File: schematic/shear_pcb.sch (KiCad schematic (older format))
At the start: 6 parts, among them J1 MOTOR1, J2 MOTOR2, J3 LCD_CONN, U1 Teensy3.5, U2 AMIS30542, U3 AMIS30542

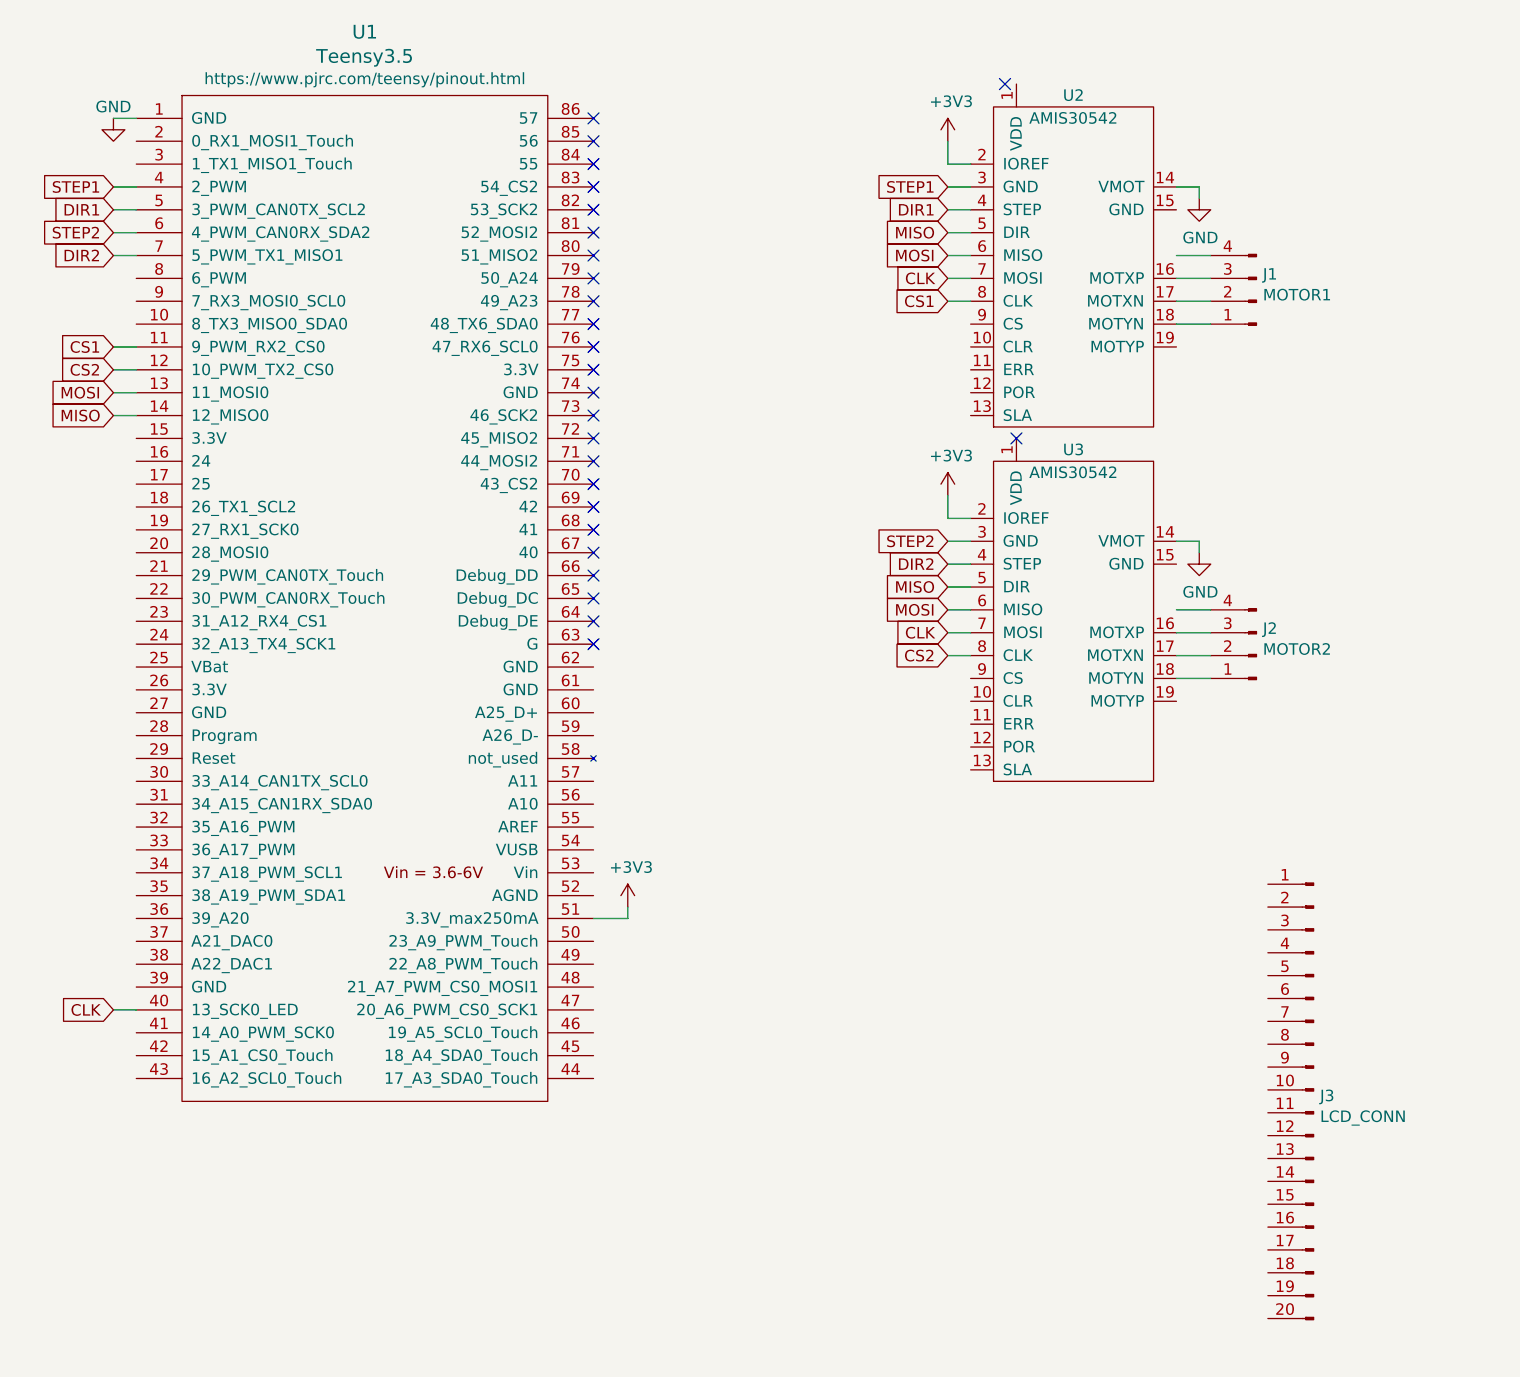
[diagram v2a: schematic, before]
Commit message: Add connectors and first pcb design
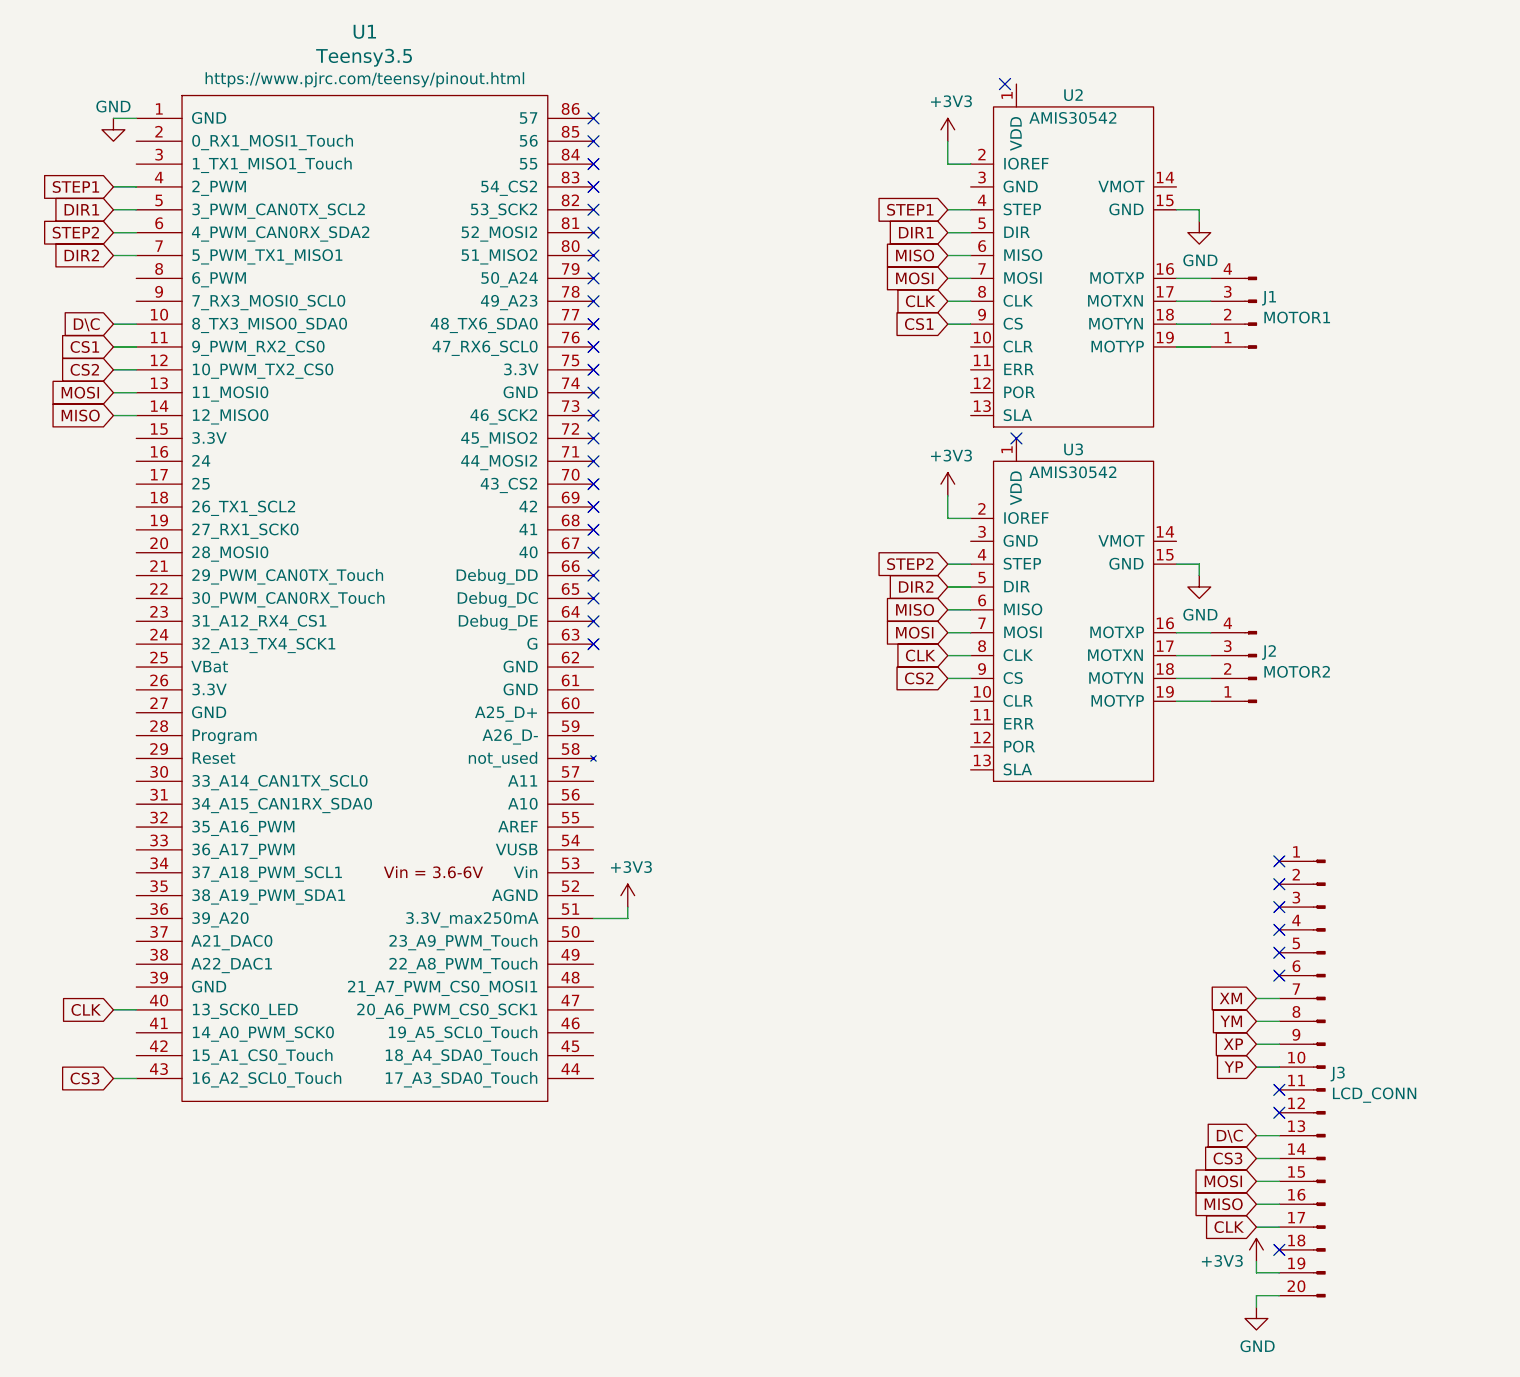
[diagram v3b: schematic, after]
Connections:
- net labels added: CS3, D\C, XM, XP, YM, YP
- wire segments 40 -> 55
- no-connect marks 26 -> 35
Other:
- moved on the sheet: J1, J2, J3
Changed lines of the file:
@@
 L power:GND #PWR0105
 U 1 1 5CCD7013
-P 9250 2950
-F 0 "#PWR0105" H 9250 2700 50  0001 C CNN
-F 1 "GND" H 9255 2777 50  0000 C CNN
-F 2 "" H 9250 2950 50  0001 C CNN
-F 3 "" H 9250 2950 50  0001 C CNN
-	1    9250 2950
+P 9250 3050
+F 0 "#PWR0105" H 9250 2800 50  0001 C CNN
+F 1 "GND" H 9255 2877 50  0000 C CNN
+F 2 "" H 9250 3050 50  0001 C CNN
+F 3 "" H 9250 3050 50  0001 C CNN
+	1    9250 3050
 	1    0    0    -1
 $EndComp
@@
 L power:GND #PWR0106
 U 1 1 5CCD743D
-P 9250 1400
-F 0 "#PWR0106" H 9250 1150 50  0001 C CNN
-F 1 "GND" H 9255 1227 50  0000 C CNN
-F 2 "" H 9250 1400 50  0001 C CNN
-F 3 "" H 9250 1400 50  0001 C CNN
-	1    9250 1400
-	1    0    0    -1
-$EndComp
-Wire Wire Line
-	9150 2900 9250 2900
-Wire Wire Line
-	9250 2900 9250 2950
-Wire Wire Line
-	9150 1350 9250 1350
-Wire Wire Line
-	9250 1350 9250 1400
+P 9250 1500
+F 0 "#PWR0106" H 9250 1250 50  0001 C CNN
+F 1 "GND" H 9255 1327 50  0000 C CNN
+F 2 "" H 9250 1500 50  0001 C CNN
+F 3 "" H 9250 1500 50  0001 C CNN
+	1    9250 1500
+	1    0    0    -1
+$EndComp
+Wire Wire Line
+	9150 3000 9250 3000
+Wire Wire Line
+	9250 3000 9250 3050
+Wire Wire Line
+	9150 1450 9250 1450
+Wire Wire Line
+	9250 1450 9250 1500
 Wire Wire Line
 	4500 1050 4600 1050
-Text GLabel 8150 3100 0    50   Input ~ 0
-MISO
 Text GLabel 8150 3200 0    50   Input ~ 0
-MOSI
-Wire Wire Line
-	8150 3100 8250 3100
-Wire Wire Line
-	8250 3200 8150 3200
-Text GLabel 8150 1550 0    50   Input ~ 0
-MISO
+MISO
+Text GLabel 8150 3300 0    50   Input ~ 0
+MOSI
+Wire Wire Line
+	8150 3200 8250 3200
+Wire Wire Line
+	8250 3300 8150 3300
 Text GLabel 8150 1650 0    50   Input ~ 0
+MISO
+Text GLabel 8150 1750 0    50   Input ~ 0
 MOSI
 Text GLabel 4500 2350 0    50   Input ~ 0
@@
 	4500 2350 4600 2350
 Wire Wire Line
-	8150 1550 8250 1550
-Wire Wire Line
 	8150 1650 8250 1650
+Wire Wire Line
+	8150 1750 8250 1750
 Text GLabel 4500 4950 0    50   Input ~ 0
 CLK
-Text GLabel 8150 3300 0    50   Input ~ 0
-CLK
-Text GLabel 8150 1750 0    50   Input ~ 0
-CLK
-Wire Wire Line
-	8150 1750 8250 1750
-Wire Wire Line
-	8250 3300 8150 3300
+Text GLabel 8150 3400 0    50   Input ~ 0
+CLK
+Text GLabel 8150 1850 0    50   Input ~ 0
+CLK
+Wire Wire Line
+	8150 1850 8250 1850
+Wire Wire Line
+	8250 3400 8150 3400
 Wire Wire Line
 	4500 4950 4600 4950
@@
 L Connector:Conn_01x04_Male J2
 U 1 1 5CCCF848
-P 9500 3400
-F 0 "J2" H 9472 3282 50  0000 R CNN
-F 1 "MOTOR2" H 9472 3373 50  0000 R CNN
-F 2 "Connector_PinHeader_2.54mm:PinHeader_1x04_P2.54mm_Vertical" H 9500 3400 50  0001 C CNN
-F 3 "~" H 9500 3400 50  0001 C CNN
-	1    9500 3400
+P 9500 3500
+F 0 "J2" H 9472 3382 50  0000 R CNN
+F 1 "MOTOR2" H 9472 3473 50  0000 R CNN
+F 2 "Connector_PinHeader_2.54mm:PinHeader_1x04_P2.54mm_Vertical" H 9500 3500 50  0001 C CNN
+F 3 "~" H 9500 3500 50  0001 C CNN
+	1    9500 3500
 	-1   0    0    1
 $EndComp
 Wire Wire Line
-	9150 3200 9300 3200
-Wire Wire Line
 	9150 3300 9300 3300
 Wire Wire Line
@@
 Wire Wire Line
 	9150 3500 9300 3500
+Wire Wire Line
+	9150 3600 9300 3600
 $Comp
 L Connector:Conn_01x04_Male J1
 U 1 1 5CCD4004
-P 9500 1850
-F 0 "J1" H 9472 1732 50  0000 R CNN
-F 1 "MOTOR1" H 9472 1823 50  0000 R CNN
-F 2 "Connector_PinHeader_2.54mm:PinHeader_1x04_P2.54mm_Vertical" H 9500 1850 50  0001 C CNN
-F 3 "~" H 9500 1850 50  0001 C CNN
-	1    9500 1850
+P 9500 1950
+F 0 "J1" H 9472 1832 50  0000 R CNN
+F 1 "MOTOR1" H 9472 1923 50  0000 R CNN
+F 2 "Connector_PinHeader_2.54mm:PinHeader_1x04_P2.54mm_Vertical" H 9500 1950 50  0001 C CNN
+F 3 "~" H 9500 1950 50  0001 C CNN
+	1    9500 1950
 	-1   0    0    1
 $EndComp
-Wire Wire Line
-	9150 1650 9300 1650
 Wire Wire Line
 	9150 1750 9300 1750
@@
 Wire Wire Line
 	4500 2050 4600 2050
-Text GLabel 8150 1850 0    50   Input ~ 0
+Text GLabel 8150 1950 0    50   Input ~ 0
 CS1
-Text GLabel 8150 3400 0    50   Input ~ 0
+Text GLabel 8150 3500 0    50   Input ~ 0
 CS2
 Wire Wire Line
-	8150 3400 8250 3400
-Wire Wire Line
-	8150 1850 8250 1850
+	8150 3500 8250 3500
+Wire Wire Line
+	8150 1950 8250 1950
 Text GLabel 4500 1350 0    50   Input ~ 0
 STEP1
@@
 Wire Wire Line
 	4600 1650 4500 1650
-Text GLabel 8150 1350 0    50   Input ~ 0
+Text GLabel 8150 1450 0    50   Input ~ 0
 STEP1
-Text GLabel 8150 1450 0    50   Input ~ 0
+Text GLabel 8150 1550 0    50   Input ~ 0
 DIR1
 Wire Wire Line
-	8150 1350 8250 1350
-Wire Wire Line
-	8250 1450 8150 1450
-Text GLabel 8150 2900 0    50   Input ~ 0
+	8150 1450 8250 1450
+Wire Wire Line
+	8250 1550 8150 1550
+Text GLabel 8150 3000 0    50   Input ~ 0
 STEP2
-Text GLabel 8150 3000 0    50   Input ~ 0
+Text GLabel 8150 3100 0    50   Input ~ 0
 DIR2
 Wire Wire Line
-	8250 2900 8150 2900
-Wire Wire Line
 	8250 3000 8150 3000
+Wire Wire Line
+	8250 3100 8150 3100
 $Comp
 L Connector:Conn_01x20_Male J3
 U 1 1 5CCDF0A1
-P 9750 5300
-F 0 "J3" H 9722 5274 50  0000 R CNN
-F 1 "LCD_CONN" H 9722 5183 50  0000 R CNN
-F 2 "Connector_PinHeader_2.54mm:PinHeader_1x20_P2.54mm_Vertical" H 9750 5300 50  0001 C CNN
-F 3 "~" H 9750 5300 50  0001 C CNN
-	1    9750 5300
+P 9800 5200
+F 0 "J3" H 9772 5174 50  0000 R CNN
+F 1 "LCD_CONN" H 9772 5083 50  0000 R CNN
+F 2 "Connector_PinHeader_2.54mm:PinHeader_1x20_P2.54mm_Vertical" H 9800 5200 50  0001 C CNN
+F 3 "~" H 9800 5200 50  0001 C CNN
+	1    9800 5200
 	-1   0    0    -1
 $EndComp
@@
 NoConn ~ 6600 1150
 NoConn ~ 6600 1050
+NoConn ~ 9600 4300
+NoConn ~ 9600 4400
+NoConn ~ 9600 4500
+NoConn ~ 9600 4600
+NoConn ~ 9600 4700
+NoConn ~ 9600 4800
+Text GLabel 9500 4900 0    50   Input ~ 0
+XM
+Text GLabel 9500 5000 0    50   Input ~ 0
+YM
+Text GLabel 9500 5100 0    50   Input ~ 0
+XP
+Text GLabel 9500 5200 0    50   Input ~ 0
+YP
+Wire Wire Line
+	9600 5200 9500 5200
+Wire Wire Line
+	9500 5100 9600 5100
+Wire Wire Line
+	9600 5000 9500 5000
+Wire Wire Line
+	9500 4900 9600 4900
+Text GLabel 9500 5600 0    50   Input ~ 0
+CS3
+Text GLabel 9500 5700 0    50   Input ~ 0
+MOSI
+Text GLabel 9500 5800 0    50   Input ~ 0
+MISO
+Text GLabel 9500 5900 0    50   Input ~ 0
+CLK
+Wire Wire Line
+	9500 5600 9600 5600
+Wire Wire Line
+	9500 5700 9600 5700
+Wire Wire Line
+	9500 5800 9600 5800
+Wire Wire Line
+	9500 5900 9600 5900
+NoConn ~ 9600 6000
+NoConn ~ 9600 5300
+NoConn ~ 9600 5400
+$Comp
+L power:+3V3 #PWR0107
+U 1 1 5CD1B29D
+P 9500 6050
+F 0 "#PWR0107" H 9500 5900 50  0001 C CNN
+F 1 "+3V3" H 9350 6050 50  0000 C CNN
+F 2 "" H 9500 6050 50  0001 C CNN
+F 3 "" H 9500 6050 50  0001 C CNN
+	1    9500 6050
+	1    0    0    -1
+$EndComp
+$Comp
+L power:GND #PWR0108
+U 1 1 5CD1C2CA
+P 9500 6250
+F 0 "#PWR0108" H 9500 6000 50  0001 C CNN
+F 1 "GND" H 9505 6077 50  0000 C CNN
+F 2 "" H 9500 6250 50  0001 C CNN
+F 3 "" H 9500 6250 50  0001 C CNN
+	1    9500 6250
+	1    0    0    -1
+$EndComp
+Wire Wire Line
+	9600 6100 9500 6100
+Wire Wire Line
+	9500 6100 9500 6050
+Wire Wire Line
+	9600 6200 9500 6200
+Wire Wire Line
+	9500 6200 9500 6250
+Text GLabel 9500 5500 0    50   Input ~ 0
+D\C
+Wire Wire Line
+	9500 5500 9600 5500
+Text GLabel 4500 5250 0    50   Input ~ 0
+CS3
+Wire Wire Line
+	4500 5250 4600 5250
+Text GLabel 4500 1950 0    50   Input ~ 0
+D\C
+Wire Wire Line
+	4500 1950 4600 1950
+Wire Wire Line
+	9150 2050 9300 2050
 $EndSCHEMATC

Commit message: Redesign PCB for single-side fabrication
-Add power and endstop connectors
-Add LCD connector
-Reroute SPI and step/dir tracks
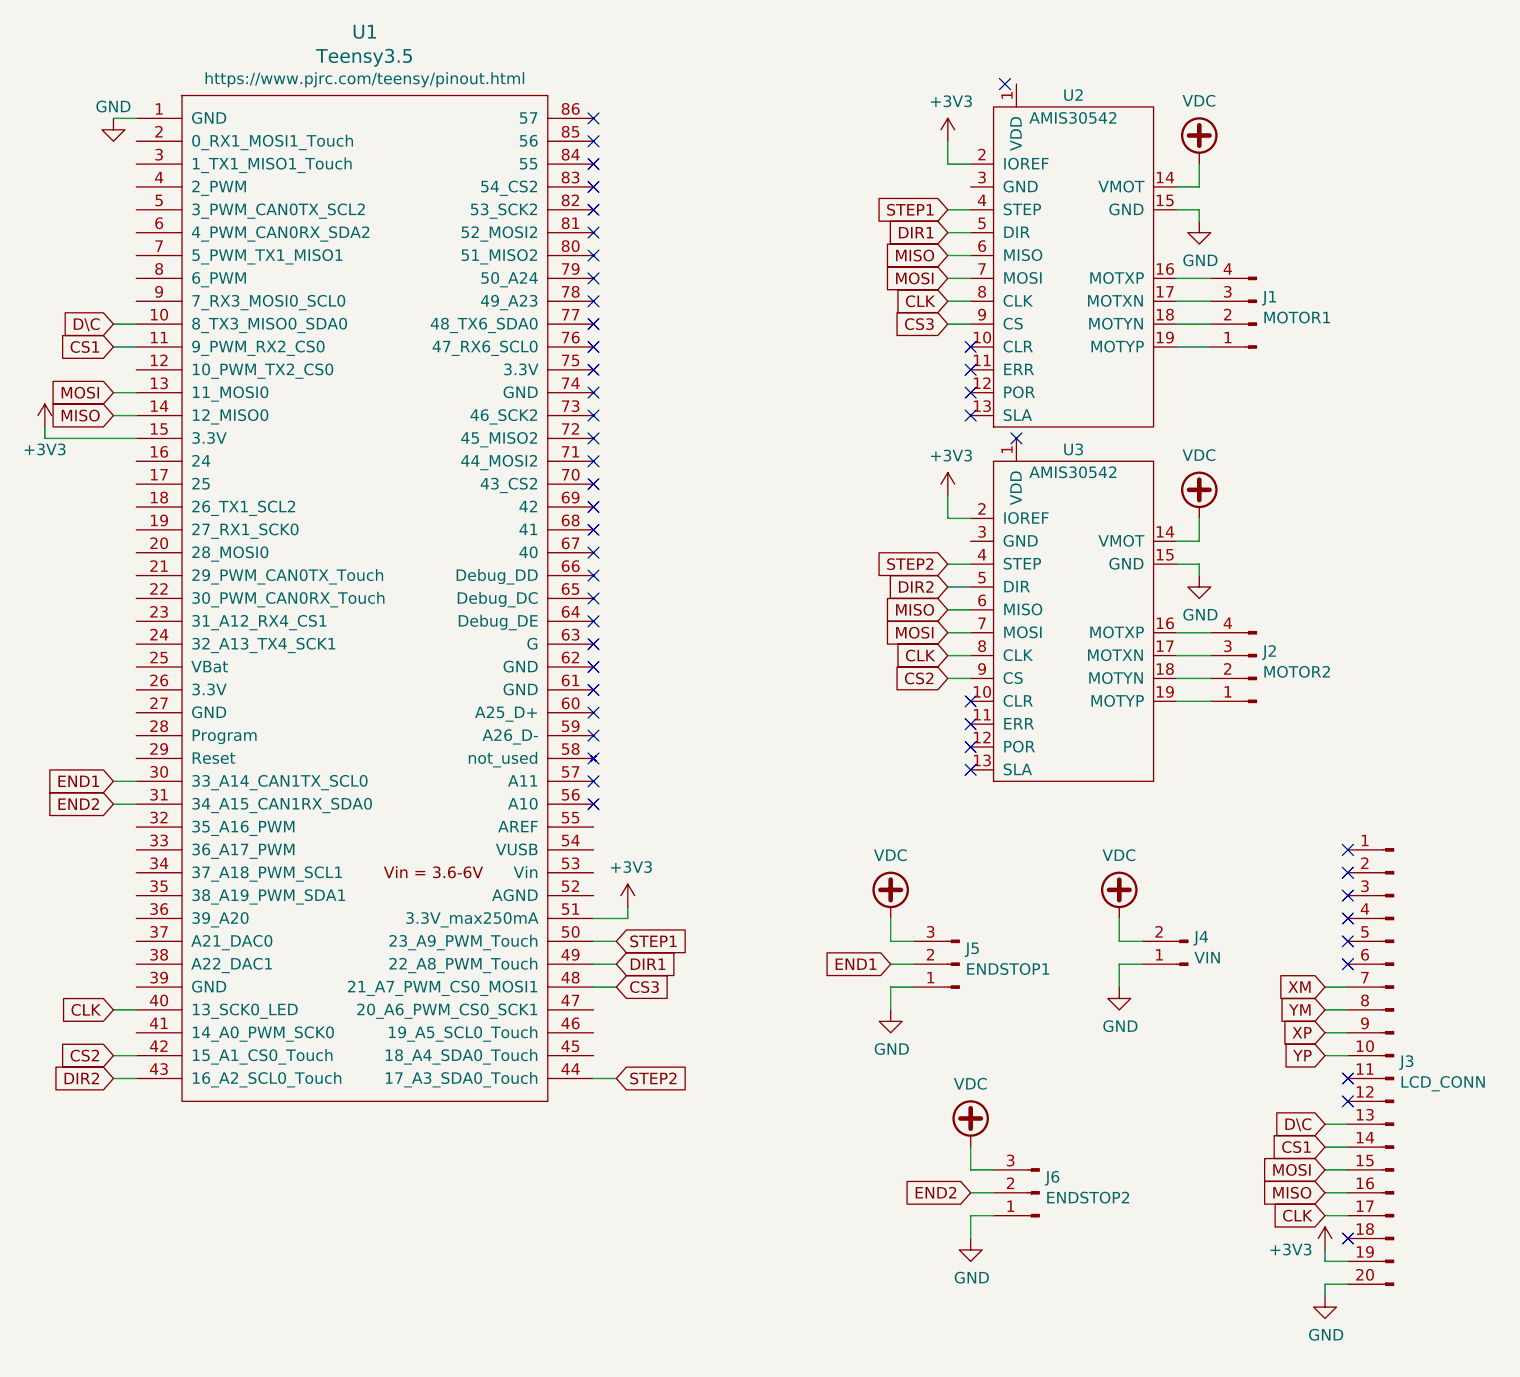
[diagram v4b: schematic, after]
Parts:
- added J4: VIN, TerminalBlock:TerminalBlock_bornier-2_P5.08mm, symbol Connector:Conn_01x02_Male
- added J5: ENDSTOP1, TerminalBlock_4Ucon:TerminalBlock_4Ucon_1x03_P3.50mm_Horizontal, symbol Connector:Conn_01x03_Male
- added J6: ENDSTOP2, TerminalBlock_4Ucon:TerminalBlock_4Ucon_1x03_P3.50mm_Horizontal, symbol Connector:Conn_01x03_Male
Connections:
- net +3V3: now also U1.15 (3.3V)
- net CS1: now also J3.14 (Pin_14); no longer U2.9 (CS)
- net CS2: now also U1.42 (15_A1_CS0_Touch); no longer U1.12 (10_PWM_TX2_CS0)
- net CS3: now also U1.48 (21_A7_PWM_CS0_MOSI1), U2.9 (CS); no longer J3.14 (Pin_14), U1.43 (16_A2_SCL0_Touch)
- net DIR1: now also U1.49 (22_A8_PWM_Touch); no longer U1.5 (3_PWM_CAN0TX_SCL2)
- net DIR2: now also U1.43 (16_A2_SCL0_Touch); no longer U1.7 (5_PWM_TX1_MISO1)
- net GND: now also J4.1 (Pin_1), J5.1 (Pin_1), J6.1 (Pin_1)
- net STEP1: now also U1.50 (23_A9_PWM_Touch); no longer U1.4 (2_PWM)
- net STEP2: now also U1.44 (17_A3_SDA0_Touch); no longer U1.6 (4_PWM_CAN0RX_SDA2)
- net END1: now reaches U1.30 (33_A14_CAN1TX_SCL0)
- net END1: now also J5.2 (Pin_2)
- net END2: now reaches U1.31 (34_A15_CAN1RX_SDA0)
- net END2: now also J6.2 (Pin_2)
- net VDC: now reaches U2.14 (VMOT)
- net VDC: now also U3.14 (VMOT), J4.2 (Pin_2), J5.3 (Pin_3), J6.3 (Pin_3)
- no-connect marks 35 -> 50
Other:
- moved on the sheet: J3
